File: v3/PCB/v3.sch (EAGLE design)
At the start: 54 parts, among them IC1 MC74HC595ADG, K1 G5Q-1-HA_DC5, K2 G5Q-1-HA_DC5, K3 G5Q-1-HA_DC5, K4 G5Q-1-HA_DC5, Q1 2N3904TA, Q2 2N3904TA, Q3 2N3904TA, Q4 2N3904TA, Q5 SFH6206-3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

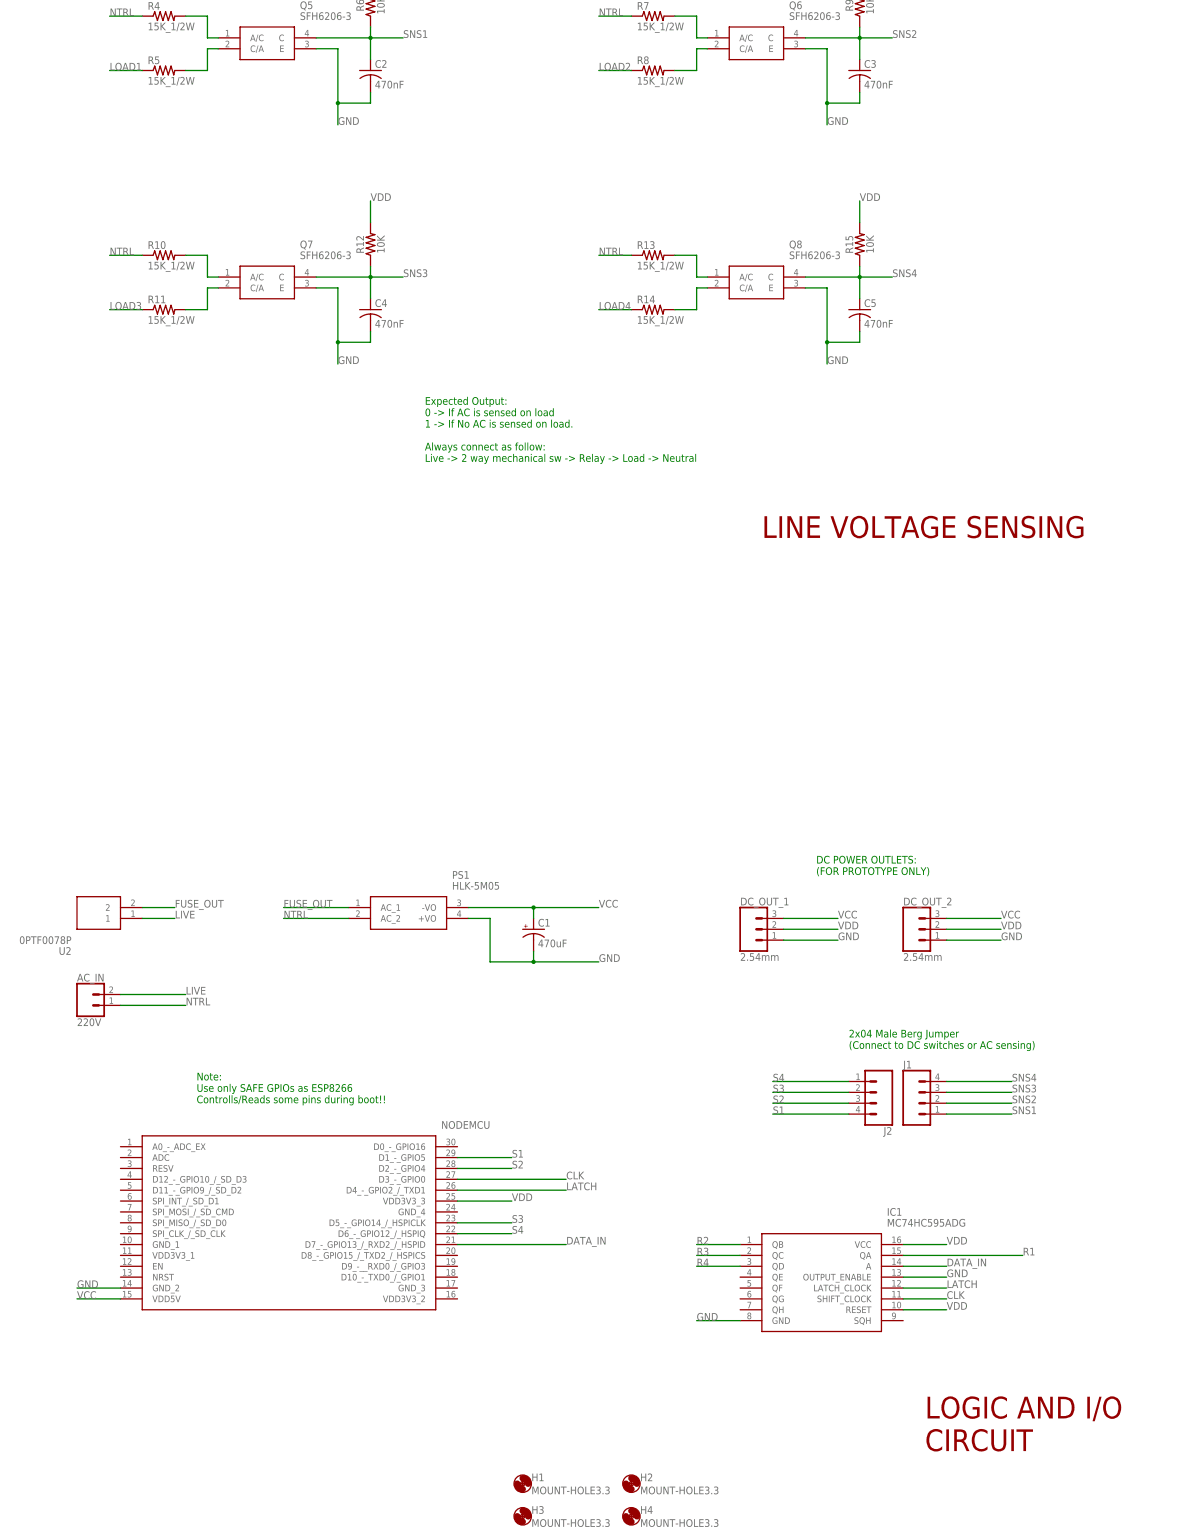
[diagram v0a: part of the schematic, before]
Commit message: v3 PCB routing completed
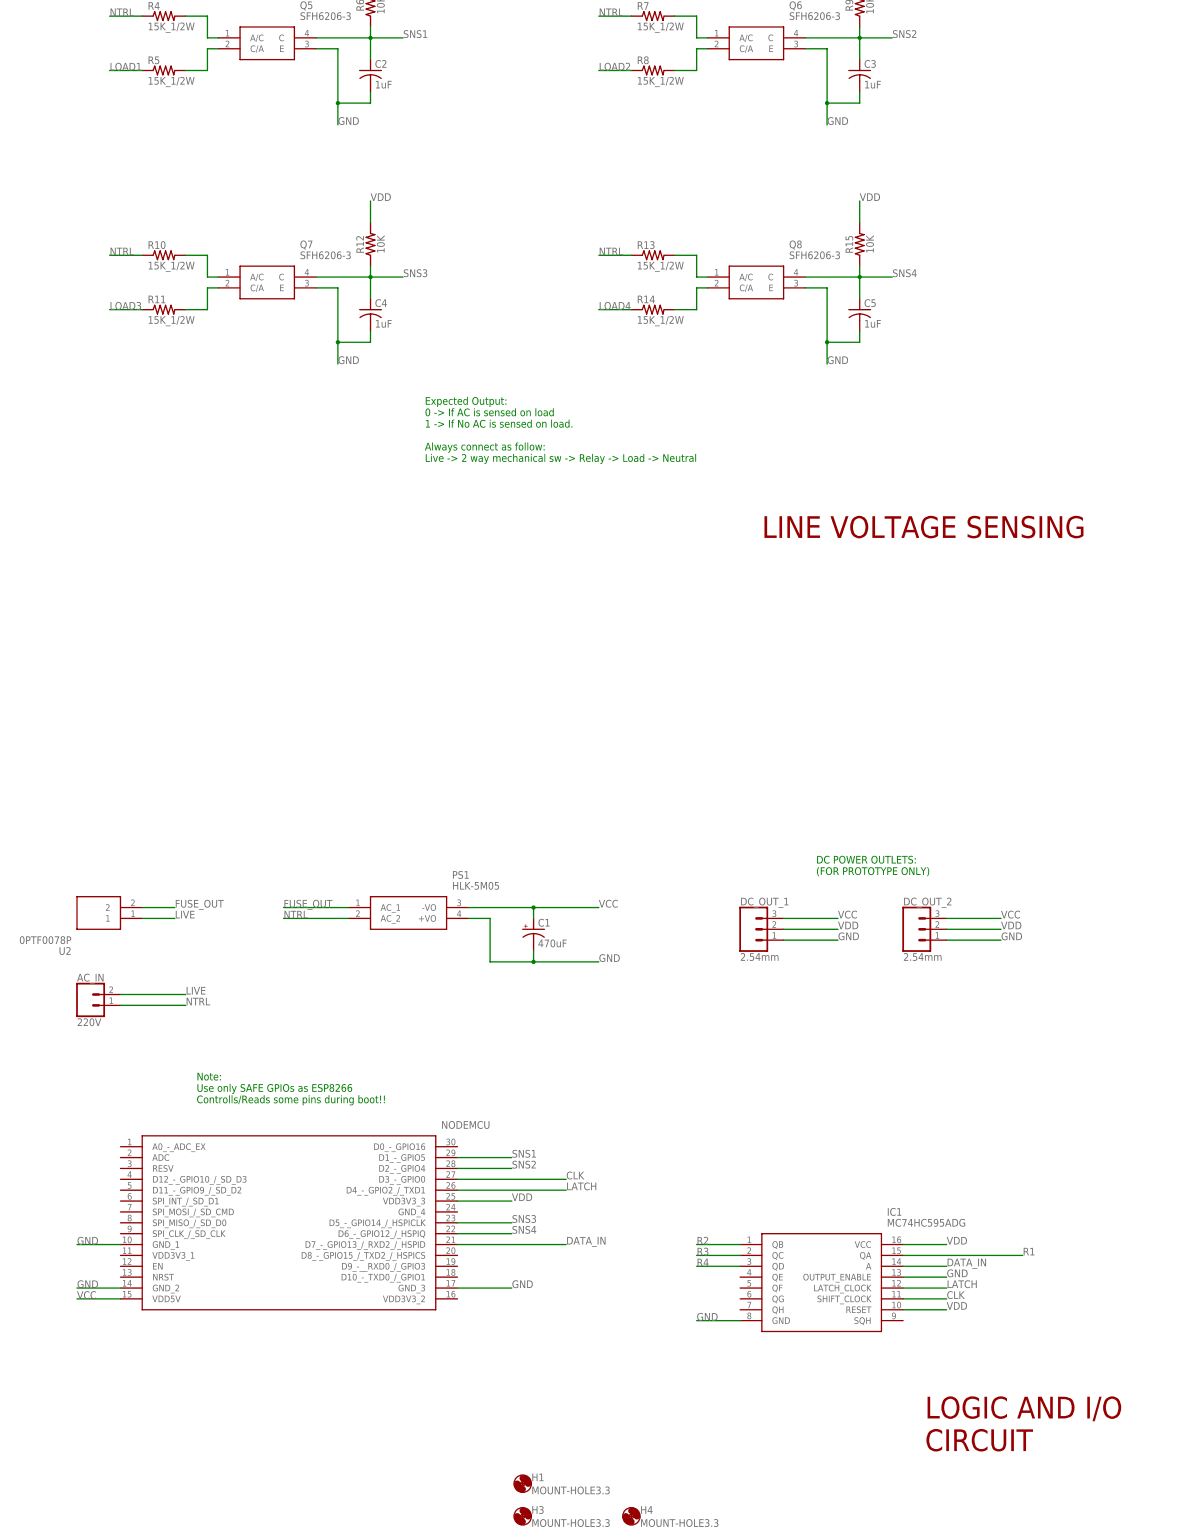
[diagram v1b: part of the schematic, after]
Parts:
- removed H2: MOUNT-HOLE3.3, holes:MOUNT-HOLE3.3
- removed J1, J2: (no value), SparkFun-Connectors:CONN_04PTH
- C2, C3, C4, C5: value 470nF -> 1uF
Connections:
- removed net S1: J2.4, NODEMCU.D1_-_GPIO5
- removed net S2: J2.3, NODEMCU.D2_-_GPIO4
- removed net S3: J2.2, NODEMCU.D5_-_GPIO14_/_HSPICLK
- removed net S4: J2.1, NODEMCU.D6_-_GPIO12_/_HSPIQ
- net GND: now also NODEMCU.GND_1, NODEMCU.GND_3
- net SNS1: now also NODEMCU.D1_-_GPIO5; no longer J1.1
- net SNS2: now also NODEMCU.D2_-_GPIO4; no longer J1.2
- net SNS3: now also NODEMCU.D5_-_GPIO14_/_HSPICLK; no longer J1.3
- net SNS4: now also NODEMCU.D6_-_GPIO12_/_HSPIQ; no longer J1.4
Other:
- note removed: "2x04 Male Berg Jumper (Connect to DC switches or AC sensing)"
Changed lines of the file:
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@@
 <?xml version="1.0" encoding="utf-8"?>
 <!DOCTYPE eagle SYSTEM "eagle.dtd">
-<eagle version="9.6.2">
+<eagle version="9.6.0">
 <drawing>
 <settings>
@@
 <part name="FRAME3" library="SparkFun-Aesthetics" deviceset="FRAME-A4L" device=""/>
 <part name="H1" library="holes" deviceset="MOUNT-HOLE" device="3.3" value="MOUNT-HOLE3.3"/>
-<part name="H2" library="holes" deviceset="MOUNT-HOLE" device="3.3" value="MOUNT-HOLE3.3"/>
 <part name="H3" library="holes" deviceset="MOUNT-HOLE" device="3.3" value="MOUNT-HOLE3.3"/>
 <part name="H4" library="holes" deviceset="MOUNT-HOLE" device="3.3" value="MOUNT-HOLE3.3"/>
@@
 <part name="R5" library="rcl" library_urn="urn:adsk.eagle:library:334" deviceset="R-US_" device="R1210" package3d_urn="urn:adsk.eagle:package:23554/2" value="15K_1/2W"/>
 <part name="R6" library="SparkFun-Resistors" deviceset="1KOHM" device="-0603-1/10W-1%" value="10K"/>
-<part name="C2" library="rcl" library_urn="urn:adsk.eagle:library:334" deviceset="C-US" device="C0805" package3d_urn="urn:adsk.eagle:package:23617/2" value="470nF"/>
+<part name="C2" library="rcl" library_urn="urn:adsk.eagle:library:334" deviceset="C-US" device="C0805" package3d_urn="urn:adsk.eagle:package:23617/2" value="1uF"/>
 <part name="Q6" library="SamacSys_Parts" deviceset="SFH6206-3" device=""/>
 <part name="R7" library="rcl" library_urn="urn:adsk.eagle:library:334" deviceset="R-US_" device="R1210" package3d_urn="urn:adsk.eagle:package:23554/2" value="15K_1/2W"/>
 <part name="R8" library="rcl" library_urn="urn:adsk.eagle:library:334" deviceset="R-US_" device="R1210" package3d_urn="urn:adsk.eagle:package:23554/2" value="15K_1/2W"/>
 <part name="R9" library="SparkFun-Resistors" deviceset="1KOHM" device="-0603-1/10W-1%" value="10K"/>
-<part name="C3" library="rcl" library_urn="urn:adsk.eagle:library:334" deviceset="C-US" device="C0805" package3d_urn="urn:adsk.eagle:package:23617/2" value="470nF"/>
+<part name="C3" library="rcl" library_urn="urn:adsk.eagle:library:334" deviceset="C-US" device="C0805" package3d_urn="urn:adsk.eagle:package:23617/2" value="1uF"/>
 <part name="Q7" library="SamacSys_Parts" deviceset="SFH6206-3" device=""/>
 <part name="R10" library="rcl" library_urn="urn:adsk.eagle:library:334" deviceset="R-US_" device="R1210" package3d_urn="urn:adsk.eagle:package:23554/2" value="15K_1/2W"/>
 <part name="R11" library="rcl" library_urn="urn:adsk.eagle:library:334" deviceset="R-US_" device="R1210" package3d_urn="urn:adsk.eagle:package:23554/2" value="15K_1/2W"/>
 <part name="R12" library="SparkFun-Resistors" deviceset="1KOHM" device="-0603-1/10W-1%" value="10K"/>
-<part name="C4" library="rcl" library_urn="urn:adsk.eagle:library:334" deviceset="C-US" device="C0805" package3d_urn="urn:adsk.eagle:package:23617/2" value="470nF"/>
+<part name="C4" library="rcl" library_urn="urn:adsk.eagle:library:334" deviceset="C-US" device="C0805" package3d_urn="urn:adsk.eagle:package:23617/2" value="1uF"/>
 <part name="Q8" library="SamacSys_Parts" deviceset="SFH6206-3" device=""/>
 <part name="R13" library="rcl" library_urn="urn:adsk.eagle:library:334" deviceset="R-US_" device="R1210" package3d_urn="urn:adsk.eagle:package:23554/2" value="15K_1/2W"/>
 <part name="R14" library="rcl" library_urn="urn:adsk.eagle:library:334" deviceset="R-US_" device="R1210" package3d_urn="urn:adsk.eagle:package:23554/2" value="15K_1/2W"/>
 <part name="R15" library="SparkFun-Resistors" deviceset="1KOHM" device="-0603-1/10W-1%" value="10K"/>
-<part name="C5" library="rcl" library_urn="urn:adsk.eagle:library:334" deviceset="C-US" device="C0805" package3d_urn="urn:adsk.eagle:package:23617/2" value="470nF"/>
-<part name="J1" library="SparkFun-Connectors" deviceset="CONN_04" device="PTH"/>
-<part name="J2" library="SparkFun-Connectors" deviceset="CONN_04" device="PTH"/>
+<part name="C5" library="rcl" library_urn="urn:adsk.eagle:library:334" deviceset="C-US" device="C0805" package3d_urn="urn:adsk.eagle:package:23617/2" value="1uF"/>
 <part name="IC1" library="SamacSys_Parts" deviceset="MC74HC595ADG" device=""/>
 </parts>
@@
 <text x="195.58" y="165.1" size="1.778" layer="91">DC POWER OUTLETS:
 (FOR PROTOTYPE ONLY)</text>
-<text x="203.2" y="124.46" size="1.778" layer="91">2x04 Male Berg Jumper
-(Connect to DC switches or AC sensing)</text>
 <text x="104.14" y="261.62" size="1.778" layer="91">Expected Output:
 0 -&gt; If AC is sensed on load
@@
 <attribute name="VALUE" x="129.032" y="20.3962" size="1.778" layer="96"/>
 </instance>
-<instance part="H2" gate="G$1" x="152.4" y="22.86" smashed="yes">
-<attribute name="NAME" x="154.432" y="23.4442" size="1.778" layer="95"/>
-<attribute name="VALUE" x="154.432" y="20.3962" size="1.778" layer="96"/>
-</instance>
 <instance part="H3" gate="G$1" x="127" y="15.24" smashed="yes">
 <attribute name="NAME" x="129.032" y="15.8242" size="1.778" layer="95"/>
@@
 <attribute name="NAME" x="206.756" y="297.815" size="1.778" layer="95"/>
 <attribute name="VALUE" x="206.756" y="292.989" size="1.778" layer="96"/>
-</instance>
-<instance part="J1" gate="J1" x="220.98" y="111.76" smashed="yes">
-<attribute name="VALUE" x="215.9" y="104.394" size="1.778" layer="96" font="vector"/>
-<attribute name="NAME" x="215.9" y="119.888" size="1.778" layer="95" font="vector"/>
-</instance>
-<instance part="J2" gate="J1" x="208.28" y="114.3" smashed="yes" rot="R180">
-<attribute name="VALUE" x="213.36" y="121.666" size="1.778" layer="96" font="vector" rot="R180"/>
-<attribute name="NAME" x="213.36" y="106.172" size="1.778" layer="95" font="vector" rot="R180"/>
 </instance>
 <instance part="IC1" gate="G$1" x="177.8" y="78.74" smashed="yes">
@@
 <label x="226.06" y="71.12" size="1.778" layer="95"/>
 </segment>
+<segment>
+<pinref part="NODEMCU" gate="G$1" pin="GND_1"/>
+<wire x1="33.02" y1="78.74" x2="22.86" y2="78.74" width="0.1524" layer="91"/>
+<label x="22.86" y="78.74" size="1.778" layer="95"/>
+</segment>
+<segment>
+<pinref part="NODEMCU" gate="G$1" pin="GND_3"/>
+<wire x1="111.76" y1="68.58" x2="124.46" y2="68.58" width="0.1524" layer="91"/>
+<label x="124.46" y="68.58" size="1.778" layer="95"/>
+</segment>
 </net>
 <net name="VCC" class="0">
@@
 </segment>
 <segment>
-<pinref part="J1" gate="J1" pin="1"/>
-<wire x1="226.06" y1="109.22" x2="241.3" y2="109.22" width="0.1524" layer="91"/>
-<label x="241.3" y="109.22" size="1.778" layer="95"/>
+<pinref part="NODEMCU" gate="G$1" pin="D1_-_GPIO5"/>
+<wire x1="111.76" y1="99.06" x2="124.46" y2="99.06" width="0.1524" layer="91"/>
+<label x="124.46" y="99.06" size="1.778" layer="95"/>
 </segment>
 </net>
@@
 </segment>
 <segment>
-<pinref part="J1" gate="J1" pin="2"/>
-<wire x1="226.06" y1="111.76" x2="241.3" y2="111.76" width="0.1524" layer="91"/>
-<label x="241.3" y="111.76" size="1.778" layer="95"/>
+<pinref part="NODEMCU" gate="G$1" pin="D2_-_GPIO4"/>
+<wire x1="111.76" y1="96.52" x2="124.46" y2="96.52" width="0.1524" layer="91"/>
+<label x="124.46" y="96.52" size="1.778" layer="95"/>
 </segment>
 </net>
@@
 </segment>
 <segment>
-<pinref part="J1" gate="J1" pin="4"/>
-<wire x1="226.06" y1="116.84" x2="241.3" y2="116.84" width="0.1524" layer="91"/>
-<label x="241.3" y="116.84" size="1.778" layer="95"/>
+<pinref part="NODEMCU" gate="G$1" pin="D6_-_GPIO12_/_HSPIQ"/>
+<wire x1="111.76" y1="81.28" x2="124.46" y2="81.28" width="0.1524" layer="91"/>
+<label x="124.46" y="81.28" size="1.778" layer="95"/>
 </segment>
 </net>
@@
 </segment>
 <segment>
-<pinref part="J1" gate="J1" pin="3"/>
-<wire x1="226.06" y1="114.3" x2="241.3" y2="114.3" width="0.1524" layer="91"/>
-<label x="241.3" y="114.3" size="1.778" layer="95"/>
-</segment>
-</net>
-<net name="S4" class="0">
-<segment>
-<pinref part="J2" gate="J1" pin="1"/>
-<wire x1="203.2" y1="116.84" x2="185.42" y2="116.84" width="0.1524" layer="91"/>
-<label x="185.42" y="116.84" size="1.778" layer="95"/>
-</segment>
-<segment>
-<pinref part="NODEMCU" gate="G$1" pin="D6_-_GPIO12_/_HSPIQ"/>
-<wire x1="111.76" y1="81.28" x2="124.46" y2="81.28" width="0.1524" layer="91"/>
-<label x="124.46" y="81.28" size="1.778" layer="95"/>
-</segment>
-</net>
-<net name="S3" class="0">
-<segment>
-<pinref part="J2" gate="J1" pin="2"/>
-<wire x1="203.2" y1="114.3" x2="185.42" y2="114.3" width="0.1524" layer="91"/>
-<label x="185.42" y="114.3" size="1.778" layer="95"/>
-</segment>
-<segment>
 <pinref part="NODEMCU" gate="G$1" pin="D5_-_GPIO14_/_HSPICLK"/>
 <wire x1="111.76" y1="83.82" x2="124.46" y2="83.82" width="0.1524" layer="91"/>
@@
 </segment>
 </net>
-<net name="S2" class="0">
-<segment>
-<pinref part="J2" gate="J1" pin="3"/>
-<wire x1="203.2" y1="111.76" x2="185.42" y2="111.76" width="0.1524" layer="91"/>
-<label x="185.42" y="111.76" size="1.778" layer="95"/>
-</segment>
-<segment>
-<pinref part="NODEMCU" gate="G$1" pin="D2_-_GPIO4"/>
-<wire x1="111.76" y1="96.52" x2="124.46" y2="96.52" width="0.1524" layer="91"/>
-<label x="124.46" y="96.52" size="1.778" layer="95"/>
-</segment>
-</net>
-<net name="S1" class="0">
-<segment>
-<pinref part="J2" gate="J1" pin="4"/>
-<wire x1="203.2" y1="109.22" x2="185.42" y2="109.22" width="0.1524" layer="91"/>
-<label x="185.42" y="109.22" size="1.778" layer="95"/>
-</segment>
-<segment>
-<pinref part="NODEMCU" gate="G$1" pin="D1_-_GPIO5"/>
-<wire x1="111.76" y1="99.06" x2="124.46" y2="99.06" width="0.1524" layer="91"/>
-<label x="124.46" y="99.06" size="1.778" layer="95"/>
-</segment>
-</net>

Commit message: OE pulled up
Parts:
- added R16: 10K, SparkFun-Resistors:1KOHM-0603-1/10W-1%
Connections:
- new net OE: IC1.OUTPUT_ENABLE, NODEMCU.D9_-__RXD0_/_GPIO3, R16.1
- net GND: no longer IC1.OUTPUT_ENABLE
- net VDD: now also R16.2
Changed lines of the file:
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@@
 <part name="C5" library="rcl" library_urn="urn:adsk.eagle:library:334" deviceset="C-US" device="C0805" package3d_urn="urn:adsk.eagle:package:23617/2" value="1uF"/>
 <part name="IC1" library="SamacSys_Parts" deviceset="MC74HC595ADG" device=""/>
+<part name="R16" library="SparkFun-Resistors" deviceset="1KOHM" device="-0603-1/10W-1%" value="10K"/>
 </parts>
 <sheets>
@@
 <attribute name="VALUE" x="212.09" y="83.82" size="1.778" layer="96" align="center-left"/>
 </instance>
+<instance part="R16" gate="G$1" x="256.54" y="71.12" smashed="yes" rot="R90">
+<attribute name="NAME" x="255.016" y="71.12" size="1.778" layer="95" font="vector" rot="R90" align="bottom-center"/>
+<attribute name="VALUE" x="258.064" y="71.12" size="1.778" layer="96" font="vector" rot="R90" align="top-center"/>
+</instance>
 </instances>
 <busses>
@@
 </segment>
 <segment>
-<pinref part="IC1" gate="G$1" pin="OUTPUT_ENABLE"/>
-<wire x1="215.9" y1="71.12" x2="226.06" y2="71.12" width="0.1524" layer="91"/>
-<label x="226.06" y="71.12" size="1.778" layer="95"/>
-</segment>
-<segment>
 <pinref part="NODEMCU" gate="G$1" pin="GND_1"/>
 <wire x1="33.02" y1="78.74" x2="22.86" y2="78.74" width="0.1524" layer="91"/>
@@
 <wire x1="215.9" y1="63.5" x2="226.06" y2="63.5" width="0.1524" layer="91"/>
 <label x="226.06" y="63.5" size="1.778" layer="95"/>
+</segment>
+<segment>
+<pinref part="R16" gate="G$1" pin="2"/>
+<wire x1="256.54" y1="76.2" x2="256.54" y2="83.82" width="0.1524" layer="91"/>
+<label x="256.54" y="83.82" size="1.778" layer="95"/>
 </segment>
 </net>
@@
 </segment>
 </net>
+<net name="OE" class="0">
+<segment>
+<pinref part="R16" gate="G$1" pin="1"/>
+<wire x1="256.54" y1="66.04" x2="256.54" y2="58.42" width="0.1524" layer="91"/>
+<label x="256.54" y="58.42" size="1.778" layer="95"/>
+</segment>
+<segment>
+<pinref part="IC1" gate="G$1" pin="OUTPUT_ENABLE"/>
+<wire x1="215.9" y1="71.12" x2="226.06" y2="71.12" width="0.1524" layer="91"/>
+<label x="226.06" y="71.12" size="1.778" layer="95"/>
+</segment>
+<segment>
+<pinref part="NODEMCU" gate="G$1" pin="D9_-__RXD0_/_GPIO3"/>
+<wire x1="111.76" y1="73.66" x2="137.16" y2="73.66" width="0.1524" layer="91"/>
+<label x="137.16" y="73.66" size="1.778" layer="95"/>
+</segment>
+</net>

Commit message: OE connected to D0 pin
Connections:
- net OE: now also NODEMCU.D0_-_GPIO16; no longer NODEMCU.D9_-__RXD0_/_GPIO3
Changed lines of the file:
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@@
 </segment>
 <segment>
-<pinref part="NODEMCU" gate="G$1" pin="D9_-__RXD0_/_GPIO3"/>
-<wire x1="111.76" y1="73.66" x2="137.16" y2="73.66" width="0.1524" layer="91"/>
-<label x="137.16" y="73.66" size="1.778" layer="95"/>
+<pinref part="NODEMCU" gate="G$1" pin="D0_-_GPIO16"/>
+<wire x1="111.76" y1="101.6" x2="137.16" y2="101.6" width="0.1524" layer="91"/>
+<label x="137.16" y="101.6" size="1.778" layer="95"/>
 </segment>
 </net>
